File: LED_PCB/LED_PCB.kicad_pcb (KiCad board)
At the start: 2 copper layers, 66 parts, among them J1 TEST_1P, J10 TEST_1P, J11 TEST_1P, J12 TEST_1P, J13 TEST_1P, J2 TEST_1P, J3 TEST_1P, J4 TEST_1P, J5 TEST_1P, J6 TEST_1P, J7 TEST_1P, J8 TEST_1P, J9 TEST_1P, Q1 Q_NMOS_GSD, Q2 Q_PMOS_GDS, U1 AZ1117CH-3_3TRG1, U2 ATTINY85-20SU

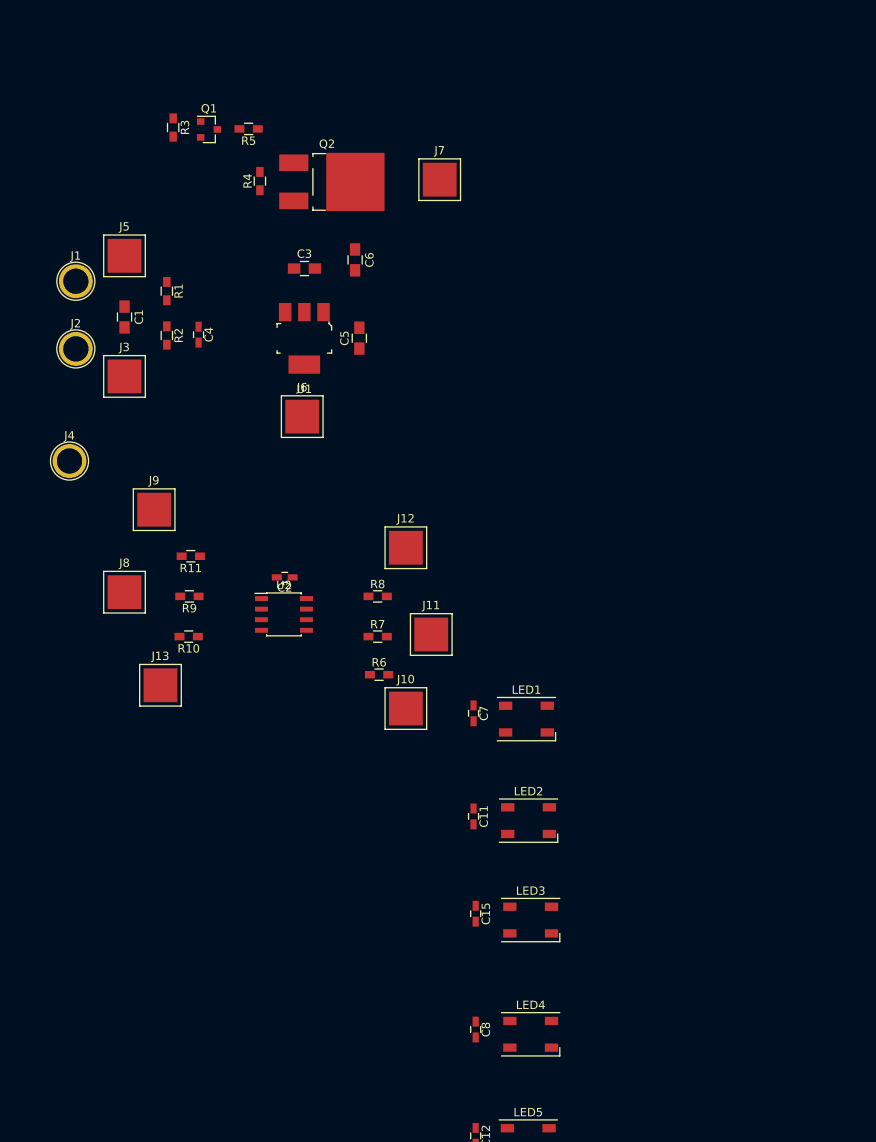
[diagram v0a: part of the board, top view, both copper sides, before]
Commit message: Added housing outline and started board outline.
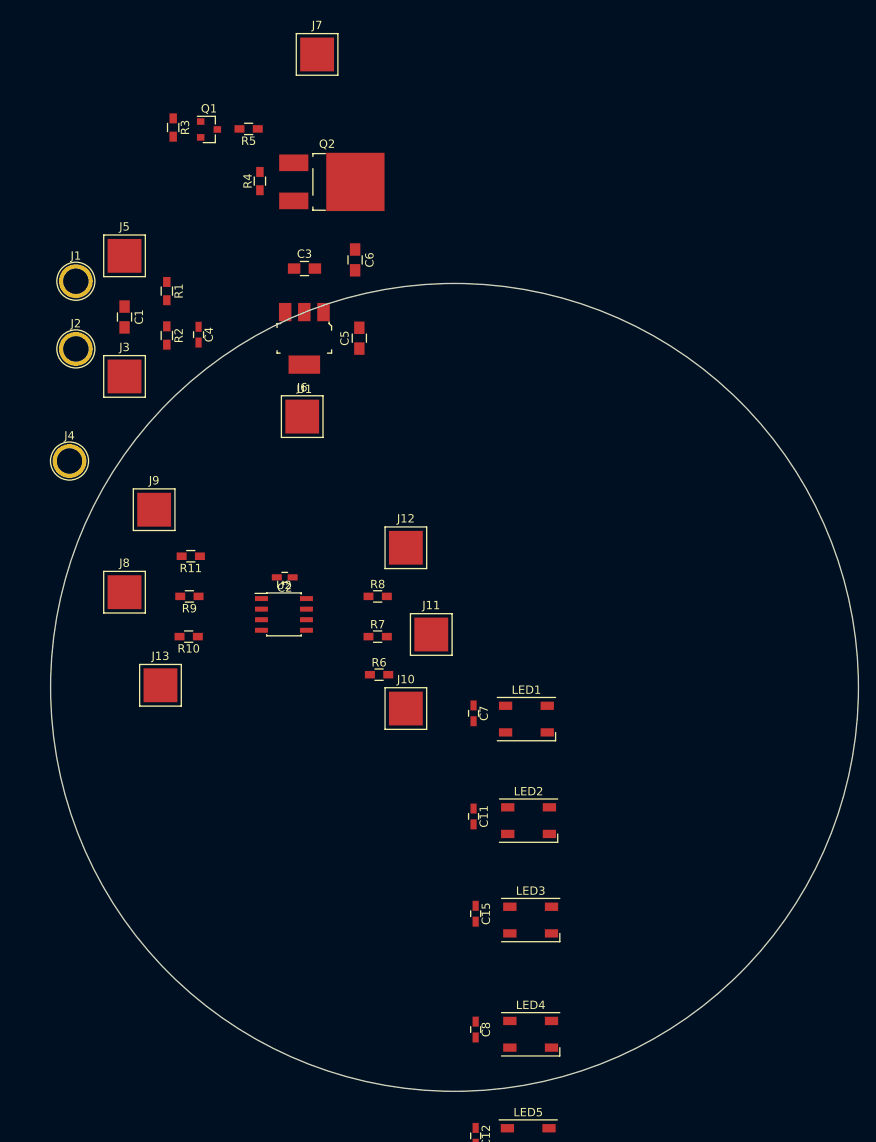
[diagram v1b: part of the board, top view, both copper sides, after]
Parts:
- moved J7 21.0 mm to (130.8, 25.6)
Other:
- board outline added: 97 x 97 mm
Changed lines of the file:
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@@
     (links 116)
     (no_connects 116)
-    (area 0 0 0 0)
+    (area 78.471429 31.135 160.439001 245.613)
     (thickness 1.6)
-    (drawings 0)
+    (drawings 9)
     (tracks 0)
     (zones 0)
@@
     (pad_drill 0.762)
     (pad_to_mask_clearance 0.2)
-    (aux_axis_origin 0 0)
-    (visible_elements FFFFFF7F)
+    (aux_axis_origin 147.32 101.6)
+    (grid_origin 147.32 101.6)
+    (visible_elements 7FFFFFFF)
     (pcbplotparams
       (layerselection 0x00030_80000001)
@@
   )
   (module SMD_Packages:1Pin (layer F.Cu)
-    (at 145.542 40.64)
+    (at 130.82 25.6)
     (descr "module 1 pin (ou trou mecanique de percage)")
     (tags DEV)
@@
     )
   )
+  (gr_circle (center 147.32 101.6) (end 193.57 101.6) (layer Eco1.User) (width 0.2))
+  (gr_line (start 171.07 191.35) (end 171.07 165.35) (layer Eco1.User) (width 0.2))
+  (gr_line (start 123.57 191.35) (end 171.07 191.35) (layer Eco1.User) (width 0.2))
+  (gr_line (start 123.57 165.35) (end 123.57 191.35) (layer Eco1.User) (width 0.2))
+  (gr_circle (center 201.87 135.55) (end 204.87 135.55) (layer Eco1.User) (width 0.2))
+  (gr_circle (center 92.77 135.55) (end 95.77 135.65) (layer Eco1.User) (width 0.2))
+  (gr_circle (center 147.32 37.35) (end 150.32 37.1) (layer Eco1.User) (width 0.2))
+  (gr_circle (center 147.32 101.6) (end 215.37 100.2) (layer Eco1.User) (width 0.2))
+  (gr_circle (center 147.32 101.6) (end 195.82 101.6) (layer Edge.Cuts) (width 0.15))
 )

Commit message: Finished board outline, and started placing LEDs
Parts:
- moved C1 217.0 mm to (-22.7, 230.5)
- moved C3 217.0 mm to (-1.09, 224.7)
- moved C4 217.0 mm to (-13.8, 232.6)
- moved C6 217.0 mm to (4.98, 223.7)
- moved J1 217.0 mm to (-28.5, 226.2)
- moved J2 217.0 mm to (-28.5, 234.4)
- moved J3 217.0 mm to (-22.7, 237.7)
- moved J4 217.0 mm to (-29.3, 247.8)
- moved J5 217.0 mm to (-22.7, 223.2)
- moved J6 217.0 mm to (-1.37, 242.5)
- moved J7 217.0 mm to (0.42, 199.0)
- moved R1 217.0 mm to (-17.6, 227.4)
- moved R2 217.0 mm to (-17.6, 232.8)
- moved R3 217.0 mm to (-16.9, 207.8)
- moved R4 217.0 mm to (-6.45, 214.2)
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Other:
- board size 97 x 97 mm -> 132.4 x 152.3 mm

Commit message: LED board: routed most of top layer... started controller PCB schematic.
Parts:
- added C19: 1000pF, Capacitors_SMD:C_0603_HandSoldering, F.Cu at (158.2, 179.6)
- added R12: 0 OHM, Resistors_SMD:R_0603_HandSoldering, F.Cu at (141.0, 175.9)
- J10, J11, J12, J13, J3, J5, J6, J7, J8: footprint SMD_Packages:1Pin -> Measurement_Points:Measurement_Point_Round-SMD-Pad_Small
- J9: value TEST_1P -> Conn_01x06; footprint SMD_Packages:1Pin -> Pin_Headers:Pin_Header_Straight_1x06_Pitch2.54mm_SMD_Pin1Left
- R11: value 1k -> 10k
- moved J4 186.6 mm to (146.1, 184.2), turned to 90 degrees
- moved J3 182.0 mm to (140.3, 156.8), turned to 90 degrees
- moved R3 178.1 mm to (157.1, 170.0), turned to 180 degrees
- moved R1 177.9 mm to (154.4, 182.1), turned to 0 degrees
- moved R2 177.9 mm to (153.8, 185.3)
- moved C4 176.0 mm to (155.7, 185.3)
- moved J2 174.4 mm to (138.4, 184.2), turned to 90 degrees
- moved Q1 171.8 mm to (155.7, 173.5), turned to 270 degrees
- moved J8 168.4 mm to (166.4, 181.6), turned to 90 degrees
- moved R5 166.2 mm to (155.7, 178.1), turned to 90 degrees
- moved C1 165.3 mm to (134.6, 179.7), turned to 0 degrees
- moved J1 164.8 mm to (130.8, 184.2), turned to 90 degrees
- moved J6 162.0 mm to (141.6, 166.4)
- moved J5 159.6 mm to (130.8, 179.7), turned to 90 degrees
- moved R11 158.9 mm to (160.1, 184.4), turned to 270 degrees
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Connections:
- C2 pad 1: +3V3 -> VCC
- C5 pad 1: +3V3 -> VCC
- J6 pad 1: +3V3 -> VCC
- J9 pad 1: Net-(J9-Pad1) -> VCC
- R11 pad 1: Net-(R11-Pad1) -> Net-(C19-Pad2)
- R11 pad 2: Net-(J9-Pad1) -> VCC
- R6 pad 1: Net-(R6-Pad1) -> Net-(J9-Pad5)
- R7 pad 1: Net-(R7-Pad1) -> Net-(J9-Pad4)
- R8 pad 1: Net-(R8-Pad1) -> Net-(J9-Pad3)
- U1 pad 2: +3V3 -> VCC
- U1 pad 4: +3V3 -> VCC
- U2 pad 1: Net-(R11-Pad1) -> Net-(C19-Pad2)
- U2 pad 5: Net-(R6-Pad1) -> Net-(J9-Pad5)
- U2 pad 6: Net-(R7-Pad1) -> Net-(J9-Pad4)
- U2 pad 7: Net-(R8-Pad1) -> Net-(J9-Pad3)
- U2 pad 8: +3V3 -> VCC
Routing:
- net Net-(D4-Pad1): track 0.00 -> 62.4 mm
- net Net-(D6-Pad1): track 0.00 -> 61.9 mm
- net Net-(C1-Pad1): track 0.00 -> 60.5 mm
- net Net-(D2-Pad1): track 0.00 -> 59.5 mm
- net Net-(LED5-Pad2): track 0.00 -> 45.0 mm
- net Net-(LED3-Pad2): track 0.00 -> 40.1 mm
- net VCC: track 0.00 -> 39.1 mm
- net Net-(LED4-Pad2): track 0.00 -> 37.3 mm
- net Net-(LED6-Pad2): track 0.00 -> 36.9 mm
- net Net-(D5-Pad1): track 0.00 -> 36.9 mm
- net Net-(LED7-Pad2): track 0.00 -> 36.3 mm
- net Net-(C19-Pad2): track 0.00 -> 34.3 mm
- net VDD: track 0.00 -> 33.9 mm
- net Net-(LED2-Pad2): track 0.00 -> 33.4 mm
- net Net-(D7-Pad1): track 0.00 -> 33.4 mm
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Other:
- copper layers 2 -> 4
- net class Default: clearance 0.2 -> 0.1524; trace_width 0.25 -> 0.3048; via_dia 0.6 -> 0.5588; via_drill 0.4 -> 0.3048
- rule trace_clearance: 0.2 -> 0.1524
- rule trace_min: 0.2 -> 0.1524
- rule via_min_drill: 0.3 -> 0.254
- rule via_min_size: 0.4 -> 0.508

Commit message: LED PCB: Changed to 2 layer, added vias and copper (not complete). Controller: Split up ESP32 and input & power sheets in schematic.
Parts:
- added REF**: VIA_12_22, CustomFootprints:VIA_12_22, F.Cu at (171.2, 149.4)
- added REF**: VIA_12_22, CustomFootprints:VIA_12_22, F.Cu at (96.3, 126.7)
- added REF**: VIA_12_22, CustomFootprints:VIA_12_22, F.Cu at (115.1, 148.8)
- added REF**: VIA_12_22, CustomFootprints:VIA_12_22, F.Cu at (158.5, 157.2)
- added REF**: VIA_12_22, CustomFootprints:VIA_12_22, F.Cu at (169.4, 152.7)
- added REF**: VIA_12_22, CustomFootprints:VIA_12_22, F.Cu at (176.5, 152.7)
- added REF**: VIA_12_22, CustomFootprints:VIA_12_22, F.Cu at (195.3, 123.4)
- added REF**: VIA_12_22, CustomFootprints:VIA_12_22, F.Cu at (196.8, 131.6)
- added REF**: VIA_12_22, CustomFootprints:VIA_12_22, F.Cu at (199.9, 103.6)
- added REF**: VIA_12_22, CustomFootprints:VIA_12_22, F.Cu at (207.8, 101.9)
- added REF**: VIA_12_22, CustomFootprints:VIA_12_22, F.Cu at (193.5, 71.4)
- added REF**: VIA_12_22, CustomFootprints:VIA_12_22, F.Cu at (191.8, 125.7)
- added REF**: VIA_12_22, CustomFootprints:VIA_12_22, F.Cu at (199.4, 71.6)
- added REF**: VIA_12_22, CustomFootprints:VIA_12_22, F.Cu at (167.9, 49.0)
- added REF**: VIA_12_22, CustomFootprints:VIA_12_22, F.Cu at (177.5, 52.3)
- added REF**: VIA_12_22, CustomFootprints:VIA_12_22, F.Cu at (137.2, 46.5)
- added REF**: VIA_12_22, CustomFootprints:VIA_12_22, F.Cu at (148.1, 49.8)
- added REF**: VIA_12_22, CustomFootprints:VIA_12_22, F.Cu at (112.5, 54.4)
- added REF**: VIA_12_22, CustomFootprints:VIA_12_22, F.Cu at (120.1, 54.1)
- added REF**: VIA_12_22, CustomFootprints:VIA_12_22, F.Cu at (100.8, 76.5)
- added REF**: VIA_12_22, CustomFootprints:VIA_12_22, F.Cu at (97.8, 67.3)
- added REF**: VIA_12_22, CustomFootprints:VIA_12_22, F.Cu at (91.9, 100.6)
- added REF**: VIA_12_22, CustomFootprints:VIA_12_22, F.Cu at (201.2, 100.1)
- added REF**: VIA_12_22, CustomFootprints:VIA_12_22, F.Cu at (88.6, 110.5)
- added REF**: VIA_12_22, CustomFootprints:VIA_12_22, F.Cu at (95.8, 128.3)
- added REF**: VIA_12_22, CustomFootprints:VIA_12_22, F.Cu at (103.1, 131.6)
- added REF**: VIA_12_22, CustomFootprints:VIA_12_22, F.Cu at (113.8, 152.1)
- added REF**: VIA_12_22, CustomFootprints:VIA_12_22, F.Cu at (123.4, 152.1)
- added REF**: VIA_12_22, CustomFootprints:VIA_12_22, F.Cu at (142.7, 157.0)
- added REF**: VIA_12_22, CustomFootprints:VIA_12_22, F.Cu at (150.9, 168.1)
- added REF**: VIA_12_22, CustomFootprints:VIA_12_22, F.Cu at (146.8, 168.1)
- added REF**: VIA_12_22, CustomFootprints:VIA_12_22, F.Cu at (148.8, 170.2)
- added REF**: VIA_12_22, CustomFootprints:VIA_12_22, F.Cu at (148.8, 166.4)
- added REF**: VIA_12_22, CustomFootprints:VIA_12_22, F.Cu at (194.8, 74.9)
- added REF**: VIA_12_22, CustomFootprints:VIA_12_22, F.Cu at (148.8, 168.1)
- added REF**: VIA_12_22, CustomFootprints:VIA_12_22, F.Cu at (132.1, 168.4)
- added REF**: VIA_12_22, CustomFootprints:VIA_12_22, F.Cu at (153.9, 171.4)
- added REF**: VIA_12_22, CustomFootprints:VIA_12_22, F.Cu at (159.5, 178.6)
- added REF**: VIA_12_22, CustomFootprints:VIA_12_22, F.Cu at (166.1, 179.6)
- added REF**: VIA_12_22, CustomFootprints:VIA_12_22, F.Cu at (152.1, 186.4)
- added REF**: VIA_12_22, CustomFootprints:VIA_12_22, F.Cu at (137.7, 180.3)
- added REF**: VIA_12_22, CustomFootprints:VIA_12_22, F.Cu at (137.7, 179.1)
- added REF**: VIA_12_22, CustomFootprints:VIA_12_22, F.Cu at (136.7, 178.3)
- added REF**: VIA_12_22, CustomFootprints:VIA_12_22, F.Cu at (135.6, 178.3)
- added REF**: VIA_12_22, CustomFootprints:VIA_12_22, F.Cu at (172.7, 49.0)
- added REF**: VIA_12_22, CustomFootprints:VIA_12_22, F.Cu at (142.7, 46.5)
- added REF**: VIA_12_22, CustomFootprints:VIA_12_22, F.Cu at (114.8, 50.8)
- added REF**: VIA_12_22, CustomFootprints:VIA_12_22, F.Cu at (96.0, 70.9)
- added REF**: VIA_12_22, CustomFootprints:VIA_12_22, F.Cu at (88.6, 105.7)
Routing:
- net GND: track 5.51 -> 69.3 mm
- net VDD: track 33.9 -> 70.9 mm
- net DIN: track 3.22 -> 38.2 mm, vias 0 -> 1
- net VCC: track 39.1 -> 53.3 mm, vias 0 -> 2
- net Net-(C1-Pad1): track 60.5 -> 65.1 mm
- added copper zone on B.Cu, net GND
- added copper zone on F.Cu, net GND
- added copper zone on B.Cu, net VDD
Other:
- copper layers 4 -> 2

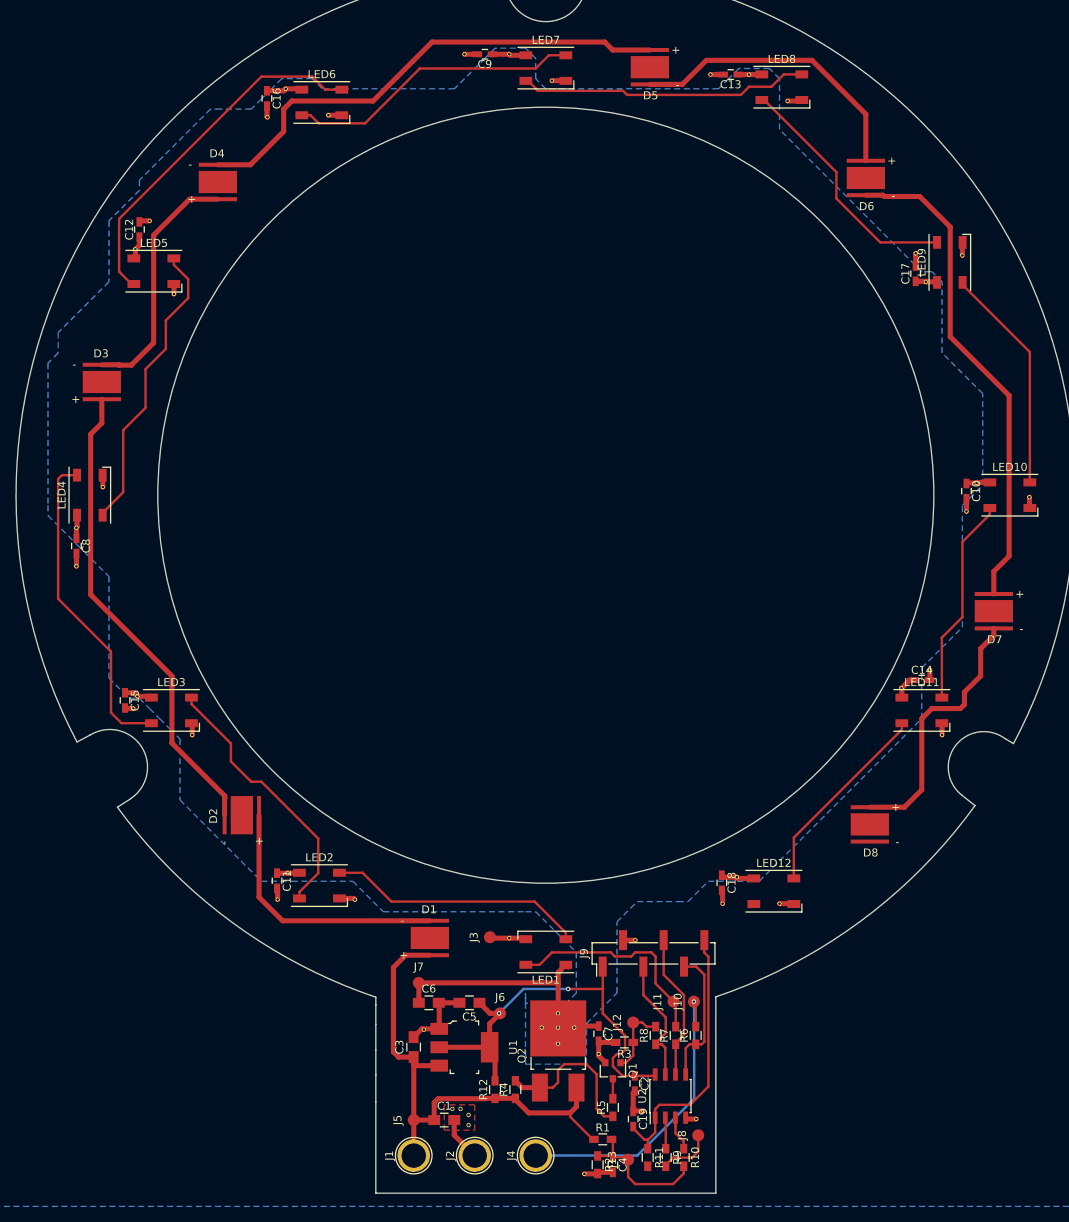
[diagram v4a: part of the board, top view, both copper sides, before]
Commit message: Added components to LED PCB sch and updated layout
Still need to add thermals for white LEDs and then run error check...
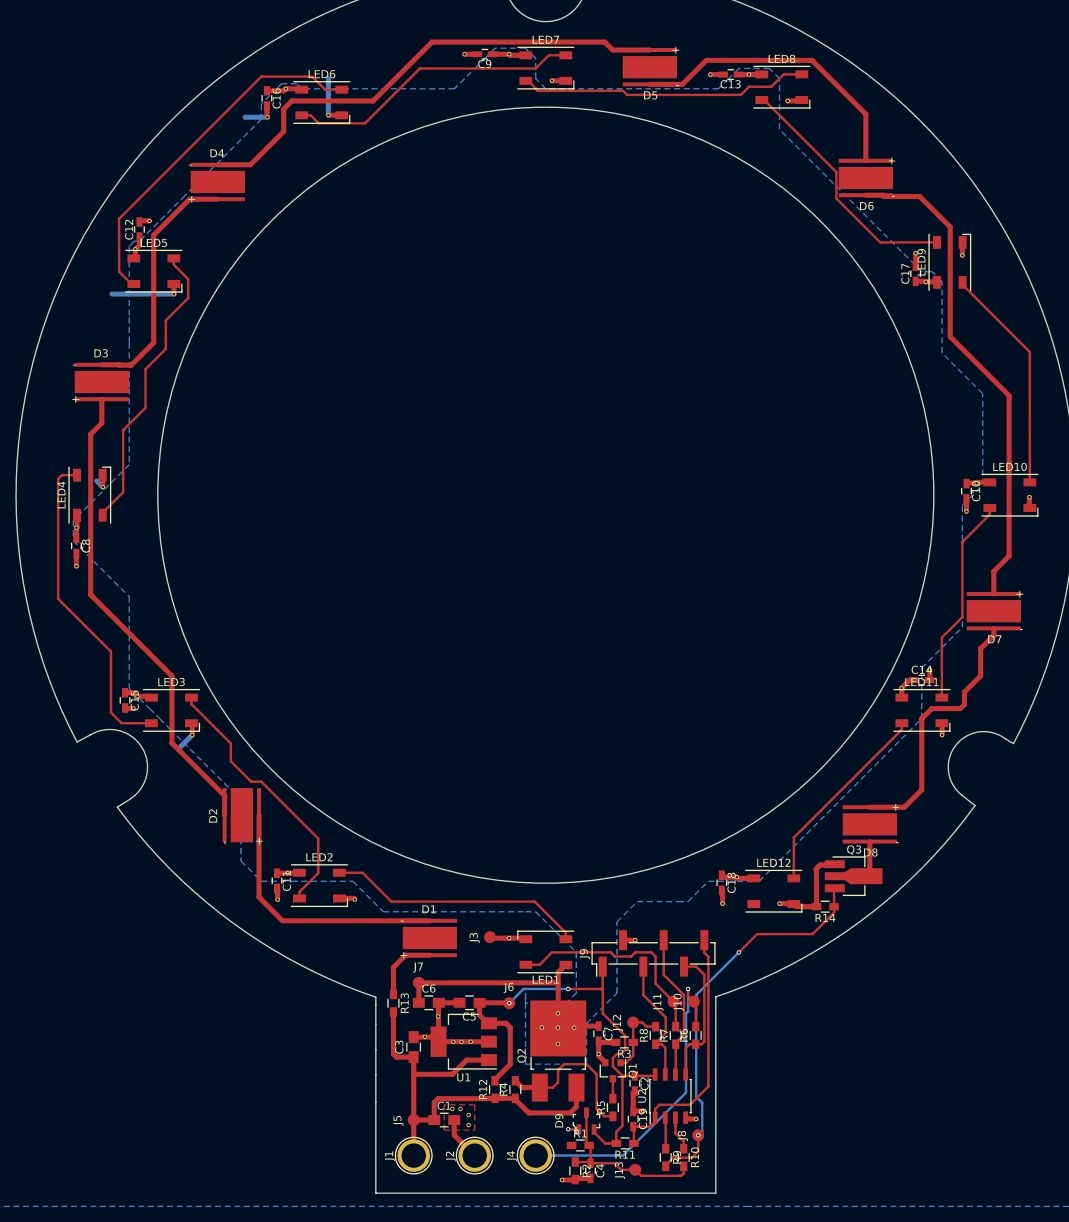
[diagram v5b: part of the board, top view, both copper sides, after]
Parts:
- added D9: BAT54S-7-F, digikey-footprints:SOT-23-3, F.Cu at (152.4, 179.8)
- added Q3: Q_NMOS_SDG, TO_SOT_Packages_SMD:SOT-89-3_Handsoldering, F.Cu at (185.4, 149.2)
- added R13: 0 OHM, Resistors_SMD:R_0603_HandSoldering, F.Cu at (128.3, 165.1)
- added R14: 10k, Resistors_SMD:R_0603_HandSoldering, F.Cu at (182.2, 153.0)
- added REF**: VIA_12_22, CustomFootprints:VIA_12_22, F.Cu at (133.9, 166.8)
- added REF**: VIA_12_22, CustomFootprints:VIA_12_22, F.Cu at (137.9, 169.9)
- added REF**: VIA_12_22, CustomFootprints:VIA_12_22, F.Cu at (136.8, 169.9)
- added REF**: VIA_12_22, CustomFootprints:VIA_12_22, F.Cu at (135.8, 169.9)
- D1, D2, D3, D4, D5, D6, D7, D8: footprint buq2:CREE-XM-L -> CustomFootprints:CREE-XM-L_HAND_SOLDERED
- U1: value AZ1117CH-3_3TRG1 -> MIC5233-3.3YS-TR; footprint digikey-footprints:SOT-223 -> TO_SOT_Packages_SMD:SOT-223
- moved R11 3.33 mm to (157.2, 182.6), turned to 180 degrees
- moved C4 2.90 mm to (152.9, 186.1)
- moved R2 2.90 mm to (151.0, 186.1)
- moved R1 2.90 mm to (151.6, 182.9)
- moved REF** 2.90 mm to (149.4, 187.2)
- moved J6 1.71 mm to (142.7, 165.1)
- moved J13 1.55 mm to (158.5, 185.9)
- moved REF** 0.90 mm to (132.2, 169.3)
- moved U1 0.70 mm to (137.1, 169.9), turned to 180 degrees
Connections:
- net MODE renamed RGB_EN
- net Net-(J8-Pad1) renamed WHITE_EN
- D1 pad 2: Net-(C1-Pad1) -> Net-(D1-Pad2)
- D1 pad 3: Net-(D1-Pad3) -> GND
- D2 pad 3: Net-(D2-Pad3) -> GND
- D3 pad 3: Net-(D3-Pad3) -> GND
- D4 pad 3: Net-(D4-Pad3) -> GND
- D5 pad 3: Net-(D5-Pad3) -> GND
- D6 pad 3: Net-(D6-Pad3) -> GND
- D7 pad 3: Net-(D7-Pad3) -> GND
- D8 pad 1: GND -> Net-(D8-Pad1)
- D8 pad 3: Net-(D8-Pad3) -> GND
- U1 pad 1: GND -> Net-(C1-Pad1)
- U1 pad 2: VCC -> GND
- U1 pad 3: Net-(C1-Pad1) -> VCC
- U1 pad 4: VCC -> GND
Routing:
- net WHITE_EN: track 6.95 -> 49.6 mm, vias 0 -> 2
- net GND: track 69.3 -> 107.3 mm, vias 0 -> 1
- net VCC: track 53.3 -> 62.5 mm
- net Net-(D1-Pad2): track 0.00 -> 8.56 mm
- net Net-(C1-Pad1): track 65.1 -> 56.9 mm
- net VIN_ADC: track 17.2 -> 21.8 mm
- net Net-(D8-Pad1): track 0.00 -> 4.50 mm
- net DIN: track 38.2 -> 40.2 mm
- net Net-(C19-Pad2): track 34.3 -> 33.2 mm
